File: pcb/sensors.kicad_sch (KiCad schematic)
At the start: 0 parts

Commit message: feat: BME280 sensor
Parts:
- added C1, C2: 100n, symbol Device:C
- added U3: BME280, Package_LGA:Bosch_LGA-8_2.5x2.5mm_P0.65mm_ClockwisePinNumbering, symbol Sensor:BME280
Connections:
- new net +3.3V: C1.1, C2.1, U3.2 (CSB), U3.6 (VDDIO), U3.8 (VDD)
- new net GND: C1.2, C2.2, U3.1 (GND), U3.5 (SDO), U3.7 (GND)
- new net I^{2}C_{SCL}: U3.4 (SCK)
- new net I^{2}C_{SDA}: U3.3 (SDI)
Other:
- note added: "Address is 0x76 when SDO is pulled low"
- note added: "C1 and C2 are to be placed as close to the VDD pins as possible"
- note added: "pp.32, ch.6.1 states that CSB must be connected to VDD_{IO} in order for the I^{2}C interface to be selected"

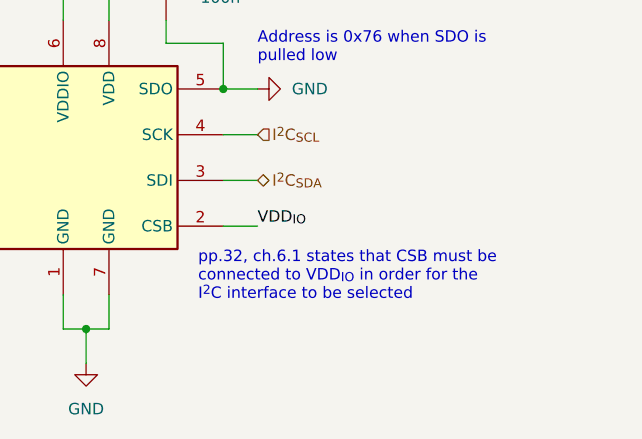
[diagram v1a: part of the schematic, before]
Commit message: fix: doc links
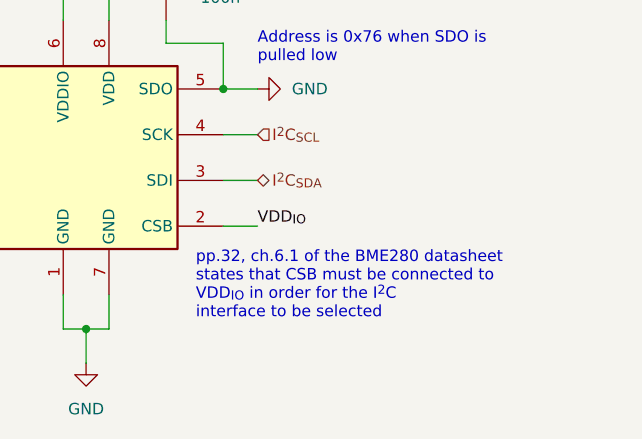
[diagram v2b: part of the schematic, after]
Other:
- note added: "pp.32, ch.6.1 of the BME280 datasheet states that CSB must be connected to VDD_{IO} in order for the I^{2}C interface to be selected"
- note removed: "pp.32, ch.6.1 states that CSB must be connected to VDD_{IO} in order for the I^{2}C interface to be selected"
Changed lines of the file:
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@@
 	(generator_version "9.0")
 	(paper "A4")
-	(text "pp.32, ch.6.1 states that CSB must be\nconnected to VDD_{IO} in order for the\nI^{2}C interface to be selected"
+	(text "pp.32, ch.6.1 of the BME280 datasheet\nstates that CSB must be connected to\nVDD_{IO} in order for the I^{2}C\ninterface to be selected"
 		(exclude_from_sim no)
-		(at 78.486 66.548 0)
+		(at 78.232 67.564 0)
 		(effects
 			(font
@@
 			)
 			(justify left)
-			(href "https://www.bosch-sensortec.com/media/boschsensortec/downloads/datasheets/bst-bme280-ds002.pdf")
+			(href "https://www.bosch-sensortec.com/media/boschsensortec/downloads/datasheets/bst-bme280-ds002.pdf#page=32")
 		)
 	)

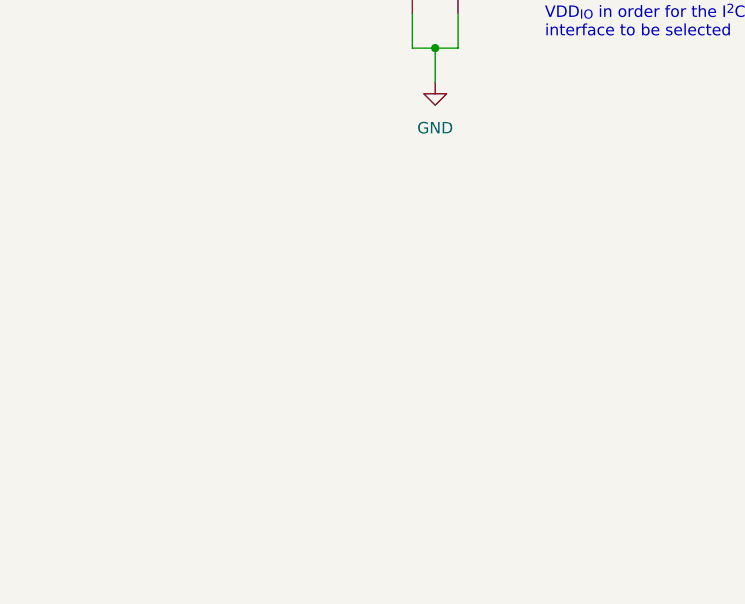
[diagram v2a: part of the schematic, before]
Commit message: feat: SGP40 sensor
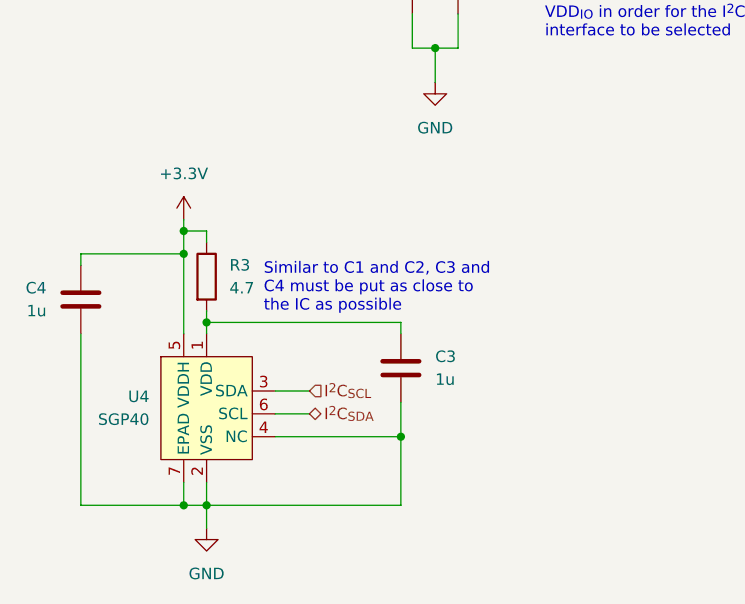
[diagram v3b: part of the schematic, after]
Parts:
- added C3, C4: 1u, symbol Device:C
- added R3: 4.7, symbol Device:R
- added U4: SGP40, Banshee:XCDR_SGP40-D-R4, symbol Banshee:SGP40
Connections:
- net +3.3V: now also C4.1, R3.1, U4.5 (VDDH)
- net GND: now also C3.2, C4.2, U4.2 (VSS), U4.4 (NC), U4.7 (EPAD)
- net I^{2}C_{SCL}: now also U4.3 (SDA)
- net I^{2}C_{SDA}: now also U4.6 (SCL)
- new net: C3.1, R3.2, U4.1 (VDD)
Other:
- note added: "Similar to C1 and C2, C3 and C4 must be put as close to the IC as possible"

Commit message: chore: organization
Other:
- note added: "BME280: Temperature, Humidity, and Barometric Pressure Sensor"
- note added: "SGP40: VOC Sensor"
- moved on the sheet: C1, C2, C3, C4, R3, U3, U4

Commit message: chore: docs
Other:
- company: (none) -> Ivan Leonard O Aparte <ivanleonard.aparte@cit.edu>
- title: (none) -> Banshee Sensor Array
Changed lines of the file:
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@@
 	(generator_version "9.0")
 	(paper "A4")
+	(title_block
+		(title "Banshee Sensor Array")
+		(date "2026-01-29")
+		(rev "1")
+		(company "Ivan Leonard O Aparte <ivanleonard.aparte@cit.edu>")
+	)
 	(text "pp.32, ch.6.1 of the BME280 datasheet\nstates that CSB must be connected to\nVDD_{IO} in order for the I^{2}C\ninterface to be selected"
 		(exclude_from_sim no)

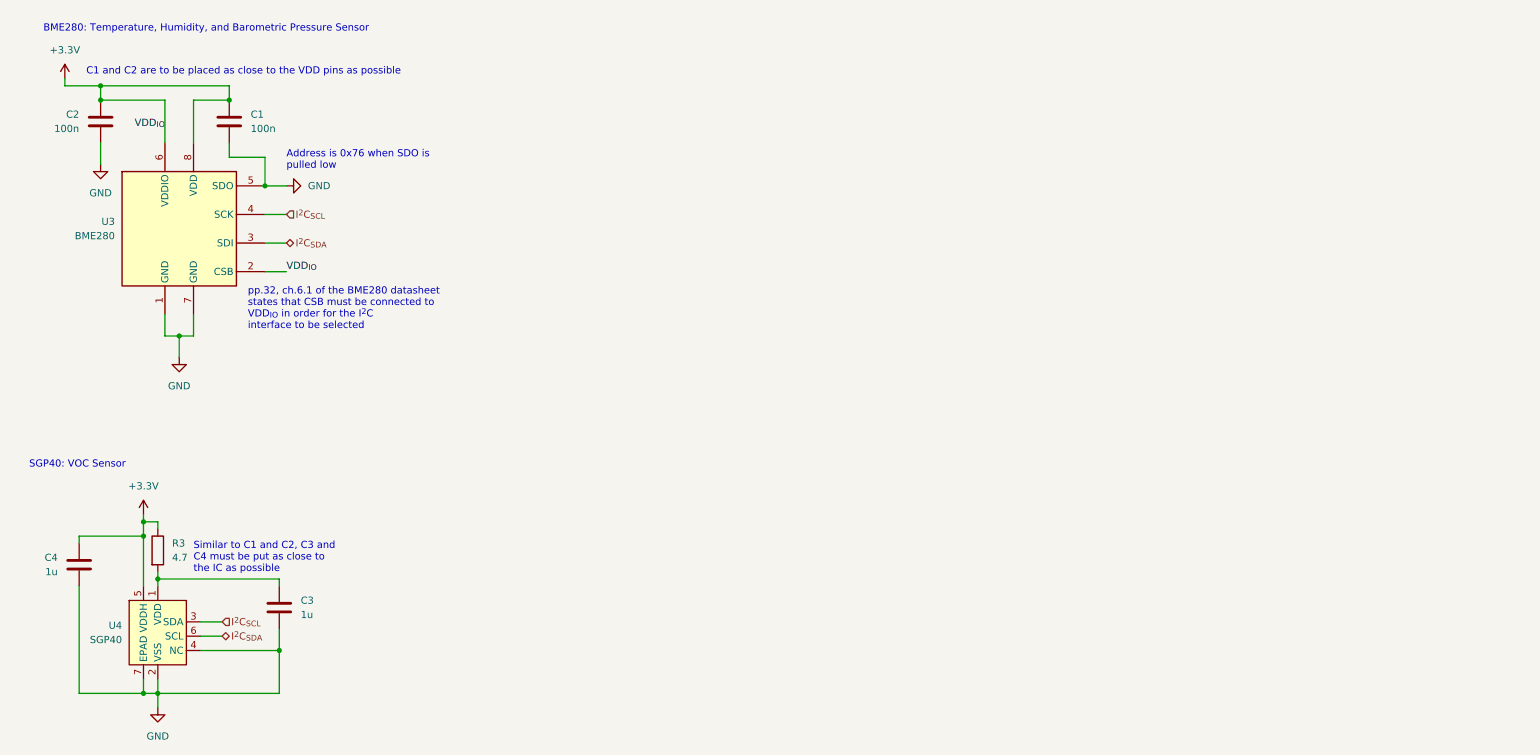
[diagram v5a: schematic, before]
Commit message: feat: anemometer & wind vane sensors
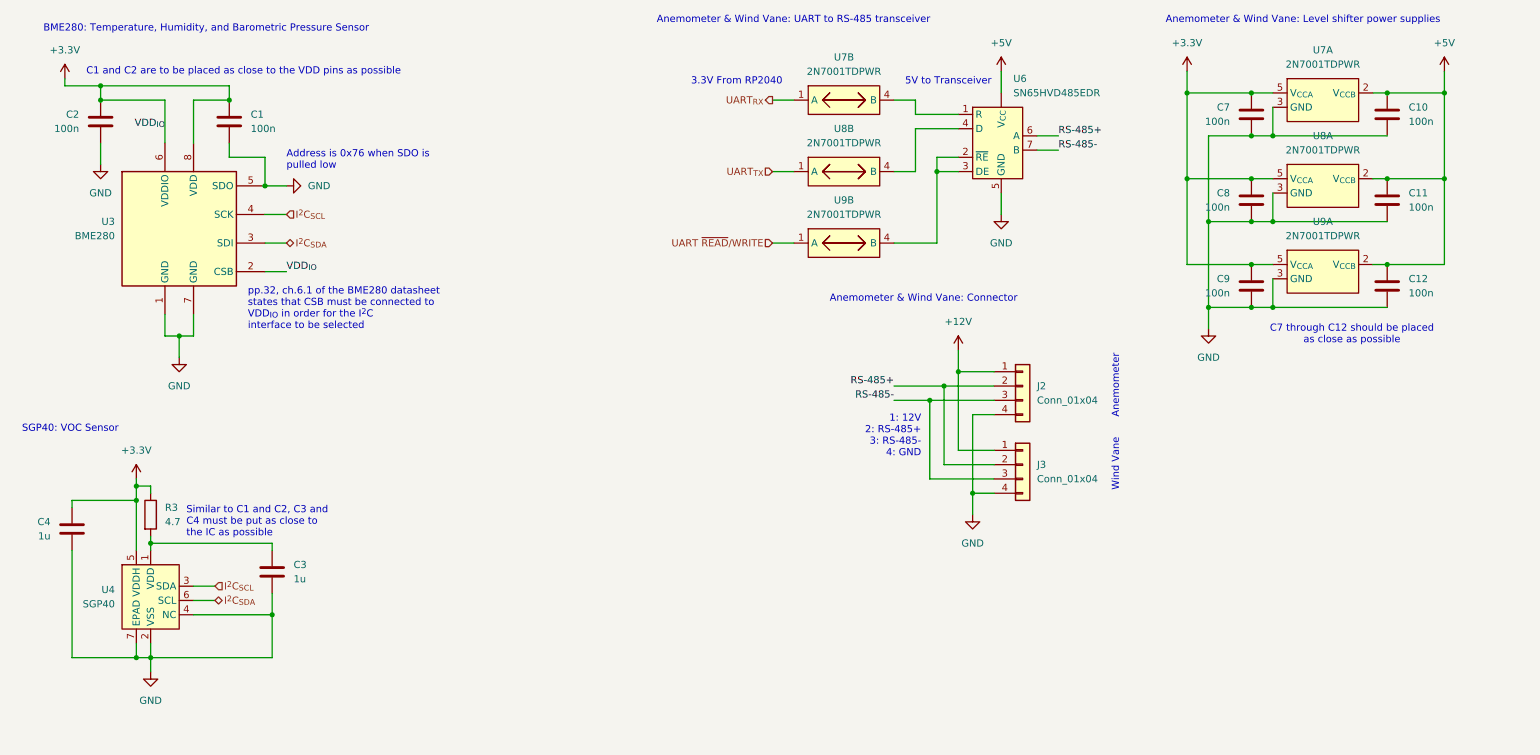
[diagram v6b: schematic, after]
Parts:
- added C10, C11, C12, C7, C8, C9: 100n, symbol Device:C
- added J2, J3: Conn_01x04, symbol Connector_Generic:Conn_01x04
- added U6: SN65HVD485EDR, Package_SO:SOIC-8_3.9x4.9mm_P1.27mm, symbol Banshee:SN65HVD485E
- added U7, U8, U9: 2N7001TDPWR, Banshee:DPW0005A, symbol Banshee:2N7001TDPWR
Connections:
- net +3.3V: now also C7.1, C8.1, C9.1, U7.5 (V_{CCA}), U8.5 (V_{CCA}), U9.5 (V_{CCA})
- net GND: now also C10.2, C11.2, C12.2, C7.2, C8.2, C9.2, J2.4 (Pin_4), J3.4 (Pin_4), U6.5 (GND), U7.3 (GND), U8.3 (GND), U9.3 (GND)
- new net: U6.1 (R), U7.4 (B)
- new net: U6.4 (D), U8.4 (B)
- new net: U6.2 (~{RE}), U6.3 (DE), U9.4 (B)
- new net +12V: J2.1 (Pin_1), J3.1 (Pin_1)
- new net +5V: C10.1, C11.1, C12.1, U6. (V_{CC}), U7.2 (V_{CCB}), U8.2 (V_{CCB}), U9.2 (V_{CCB})
- new net RS-485+: J2.2 (Pin_2), J3.2 (Pin_2), U6.6 (A)
- new net RS-485-: J2.3 (Pin_3), J3.3 (Pin_3), U6.7 (B)
- new net UART ~{READ}/WRITE: U9.1 (A)
- new net UART_{RX}: U7.1 (A)
- new net UART_{TX}: U8.1 (A)
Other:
- note added: "1: 12V 2: RS-485+ 3: RS-485- 4: GND"
- note added: "3.3V From RP2040"
- note added: "5V to Transceiver"
- note added: "Anemometer"
- note added: "Anemometer & Wind Vane: Connector"
- note added: "Anemometer & Wind Vane: Level shifter power supplies"
- note added: "Anemometer & Wind Vane: UART to RS-485 transceiver"
- note added: "C7 through C12 should be placed as close as possible"
- note added: "Wind Vane"
- moved on the sheet: C3, C4, R3, U4

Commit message: chore: swapped SGP40 for SGP41
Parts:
- removed U4: SGP40, Banshee:XCDR_SGP40-D-R4, symbol Banshee:SGP40
- added U4: SGP41, Banshee:XCDR_SGP40-D-R4, symbol Banshee:SGP41
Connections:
- net +3.3V: now also U4.5 (VDDH)
- net GND: now also U4.2 (VSS), U4.4 (NC), U4.7 (EPAD)
- net I^{2}C_{SCL}: now also U4.3 (SDA)
- net I^{2}C_{SDA}: now also U4.6 (SCL)
- net at C3.1, R3.2: now also U4.1 (VDD)
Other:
- note added: "SGP41: VOC Sensor"
- note removed: "SGP40: VOC Sensor"
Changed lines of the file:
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@@
 		)
 	)
-	(text "SGP40: VOC Sensor"
+	(text "SGP41: VOC Sensor"
 		(exclude_from_sim no)
 		(at 21.59 88.9 0)
@@
 	)
 	(symbol
-		(lib_id "Banshee:SGP40")
+		(lib_id "Banshee:SGP41")
 		(at 44.45 119.38 0)
 		(unit 1)
@@
 			)
 		)
-		(property "Value" "SGP40"
+		(property "Value" "SGP41"
 			(at 38.1 120.0149 0)
 			(effects
@@
 			)
 		)
+		(pin "2"
+		)
 		(pin "3"
 		)
+		(pin "1"
+		)
+		(pin "7"
+		)
+		(pin "5"
+		)
 		(pin "6"
 		)
-		(pin "1"
-		)
 		(pin "4"
 		)
-		(pin "2"
-		)
-		(pin "7"
-		)
-		(pin "5"
-		)
 		(instances

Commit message: chore: added note on SGP41
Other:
- note added: "Note: SGP40 is almost half the price and uses the same footprint and pinout. The only difference is that this variant also provides NO_{X} indexes"
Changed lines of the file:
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@@
+		)
+	)
+	(text "Note: SGP40 is almost half the price and uses the\nsame footprint and pinout. The only difference is\nthat this variant also provides NO_{X} indexes"
+		(exclude_from_sim no)
+		(at 83.058 93.472 0)
+		(effects
+			(font
+				(size 1.27 1.27)
+			)
+			(justify left)
 		)
 	)
